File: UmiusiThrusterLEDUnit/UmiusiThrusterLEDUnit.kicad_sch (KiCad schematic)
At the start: 5 parts, among them J1 Conn_01x04

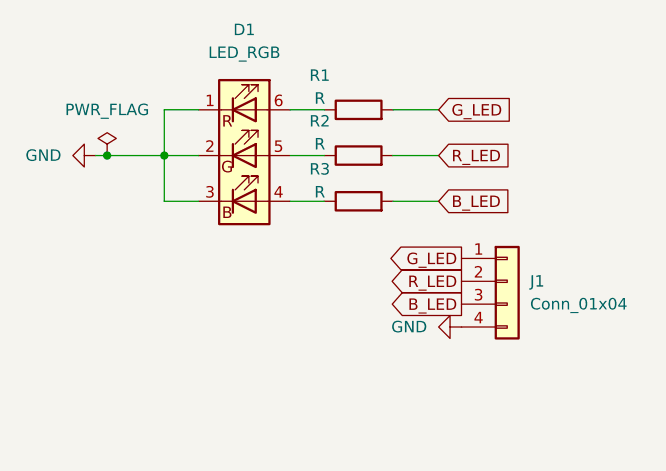
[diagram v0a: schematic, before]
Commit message: スラスターLED用基板を修正
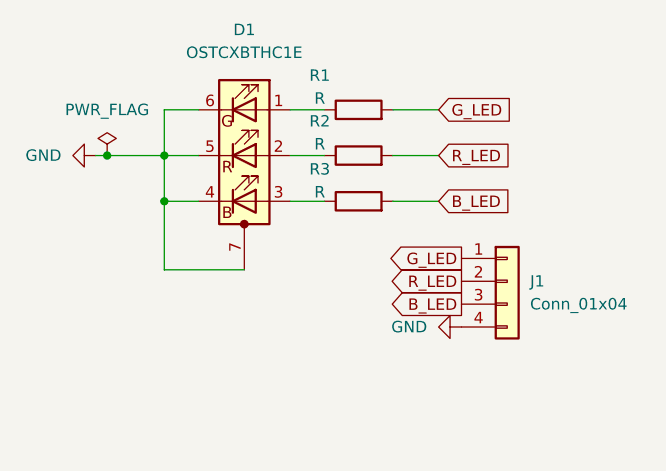
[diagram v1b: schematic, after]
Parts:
- removed D1: LED_RGB, LED_SMD:LED_RGB_5050-6, symbol Device:LED_RGB
- added D1: OSTCXBTHC1E, PowerLED:OSTCXBTHC1E, symbol PowerLED:OSTCXBTHC1E
- J1: footprint Connector_JST:JST_XH_B4B-XH-A_1x04_P2.50mm_Vertical -> Connector_PinHeader_2.54mm:PinHeader_1x04_P2.54mm_Vertical
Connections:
- net GND: now also D1.4 (BK), D1.5 (RK), D1.6 (GK), D1.7 (PAD)
- net at R3.1: now also D1.3 (BA)
- net at R2.1: now also D1.2 (RA)
- net at R1.1: now also D1.1 (GA)
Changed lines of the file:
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@@
 		(color 0 0 0 0)
 	)
+	(junction
+		(at 106.68 81.28)
+		(diameter 0)
+		(color 0 0 0 0)
+	)
 	(wire
 		(pts
@@
 	(wire
 		(pts
+			(xy 106.68 88.9) (xy 115.57 88.9)
+		)
+		(stroke
+			(width 0)
+			(type default)
+		)
+	)
+	(wire
+		(pts
 			(xy 106.68 81.28) (xy 106.68 76.2)
 		)
@@
 		(pts
 			(xy 106.68 71.12) (xy 106.68 76.2)
+		)
+		(stroke
+			(width 0)
+			(type default)
+		)
+	)
+	(wire
+		(pts
+			(xy 106.68 81.28) (xy 106.68 88.9)
 		)
 		(stroke
@@
 				(justify left)
 				(hide yes)
-			)
-		)
-	)
-	(symbol
-		(lib_id "Device:LED_RGB")
-		(at 115.57 76.2 0)
-		(unit 1)
-		(exclude_from_sim no)
-		(in_bom yes)
-		(on_board yes)
-		(dnp no)
-		(fields_autoplaced yes)
-		(property "Reference" "D1"
-			(at 115.57 62.23 0)
-			(effects
-				(font
-					(size 1.27 1.27)
-				)
-			)
-		)
-		(property "Value" "LED_RGB"
-			(at 115.57 64.77 0)
-			(effects
-				(font
-					(size 1.27 1.27)
-				)
-			)
-		)
-		(property "Footprint" "LED_SMD:LED_RGB_5050-6"
-			(at 115.57 77.47 0)
-			(effects
-				(font
-					(size 1.27 1.27)
-				)
-				(hide yes)
-			)
-		)
-		(property "Datasheet" "~"
-			(at 115.57 77.47 0)
-			(effects
-				(font
-					(size 1.27 1.27)
-				)
-				(hide yes)
-			)
-		)
-		(property "Description" "RGB LED, 6 pin package"
-			(at 115.57 76.2 0)
-			(effects
-				(font
-					(size 1.27 1.27)
-				)
-				(hide yes)
-			)
-		)
-		(pin "4"
-		)
-		(pin "5"
-		)
-		(pin "6"
-		)
-		(pin "3"
-		)
-		(pin "1"
-		)
-		(pin "2"
-		)
-		(instances
-			(project ""
-				(path "/f07b765c-e5aa-4139-8b16-07d1cd4913c5"
-					(reference "D1")
-					(unit 1)
-				)
 			)
 		)
@@
 			)
 		)
-		(property "Footprint" "Connector_JST:JST_XH_B4B-XH-A_1x04_P2.50mm_Vertical"
+		(property "Footprint" "Connector_PinHeader_2.54mm:PinHeader_1x04_P2.54mm_Vertical"
 			(at 144.78 90.17 0)
 			(effects
@@
 					(unit 1)
 				)
+			)
+		)
+	)
+	(symbol
+		(lib_id "PowerLED:OSTCXBTHC1E")
+		(at 115.57 76.2 0)
+		(unit 1)
+		(exclude_from_sim no)
+		(in_bom yes)
+		(on_board yes)
+		(dnp no)
+		(fields_autoplaced yes)
+		(property "Reference" "D1"
+			(at 115.57 62.23 0)
+			(effects
+				(font
+					(size 1.27 1.27)
+				)
+			)
+		)
+		(property "Value" "OSTCXBTHC1E"
+			(at 115.57 64.77 0)
+			(effects
+				(font
+					(size 1.27 1.27)
+				)
+			)
+		)
+		(property "Footprint" "PowerLED:OSTCXBTHC1E"
+			(at 115.57 77.47 0)
+			(effects
+				(font
+					(size 1.27 1.27)
+				)
+				(hide yes)
+			)
+		)
+		(property "Datasheet" "~"
+			(at 115.57 77.47 0)
+			(effects
+				(font
+					(size 1.27 1.27)
+				)
+				(hide yes)
+			)
+		)
+		(property "Description" "RGB LED, 6 pin package with exposed pad"
+			(at 115.57 76.2 0)
+			(effects
+				(font
+					(size 1.27 1.27)
+				)
+				(hide yes)
+			)
+		)
+		(pin "7"
+		)
+		(pin "6"
+		)
+		(pin "3"
+		)
+		(pin "1"
+		)
+		(pin "2"
+		)
+		(pin "5"
+		)
+		(pin "4"
+		)
+		(instances
+			(project ""
+				(path "/f07b765c-e5aa-4139-8b16-07d1cd4913c5"
+					(reference "D1")
+					(unit 1)
+				)

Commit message: スラスタLED基盤　REV02作成
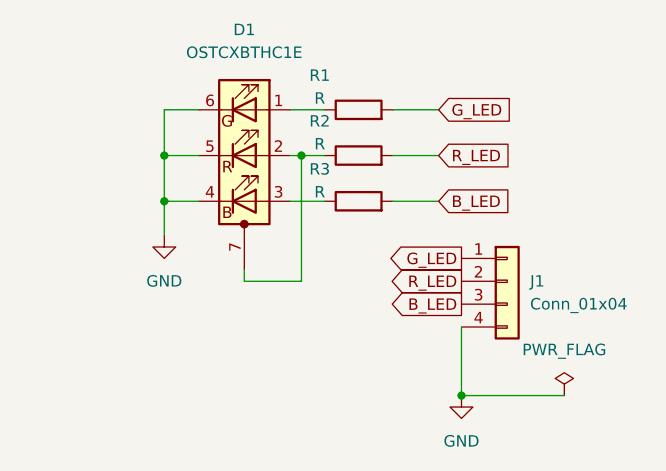
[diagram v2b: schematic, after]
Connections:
- net GND: no longer D1.7 (PAD)
- net at D1.2 (RA), R2.1: now also D1.7 (PAD)
